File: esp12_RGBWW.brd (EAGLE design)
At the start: 53 x 47 mm, 36 parts, among them Q1 AOD2910SMD, Q2 AOD2910SMD, Q3 AOD2910SMD, Q4 AOD2910SMD, Q5 AOD2910SMD, U1 TPS5410DR

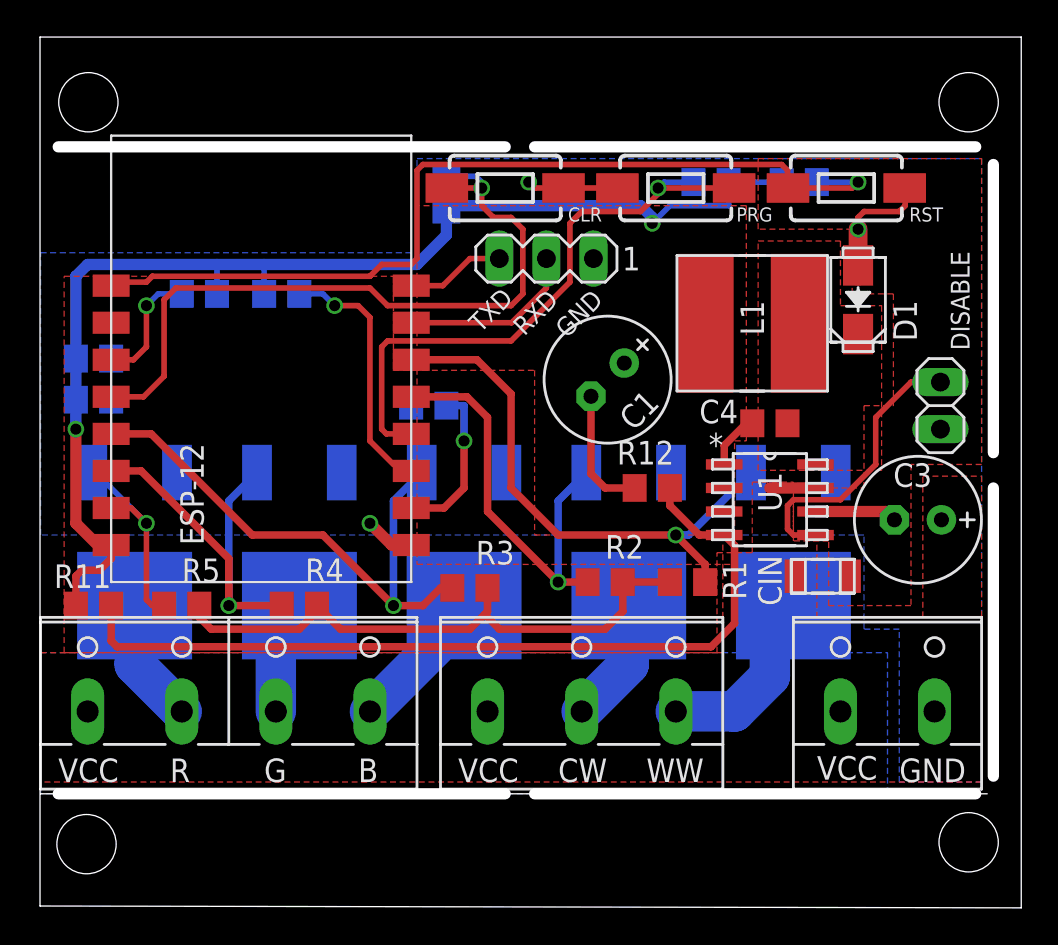
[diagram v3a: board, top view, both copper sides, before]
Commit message: minor changes
increased the size of the button text
very minor re-route of GPIO2 to resistor
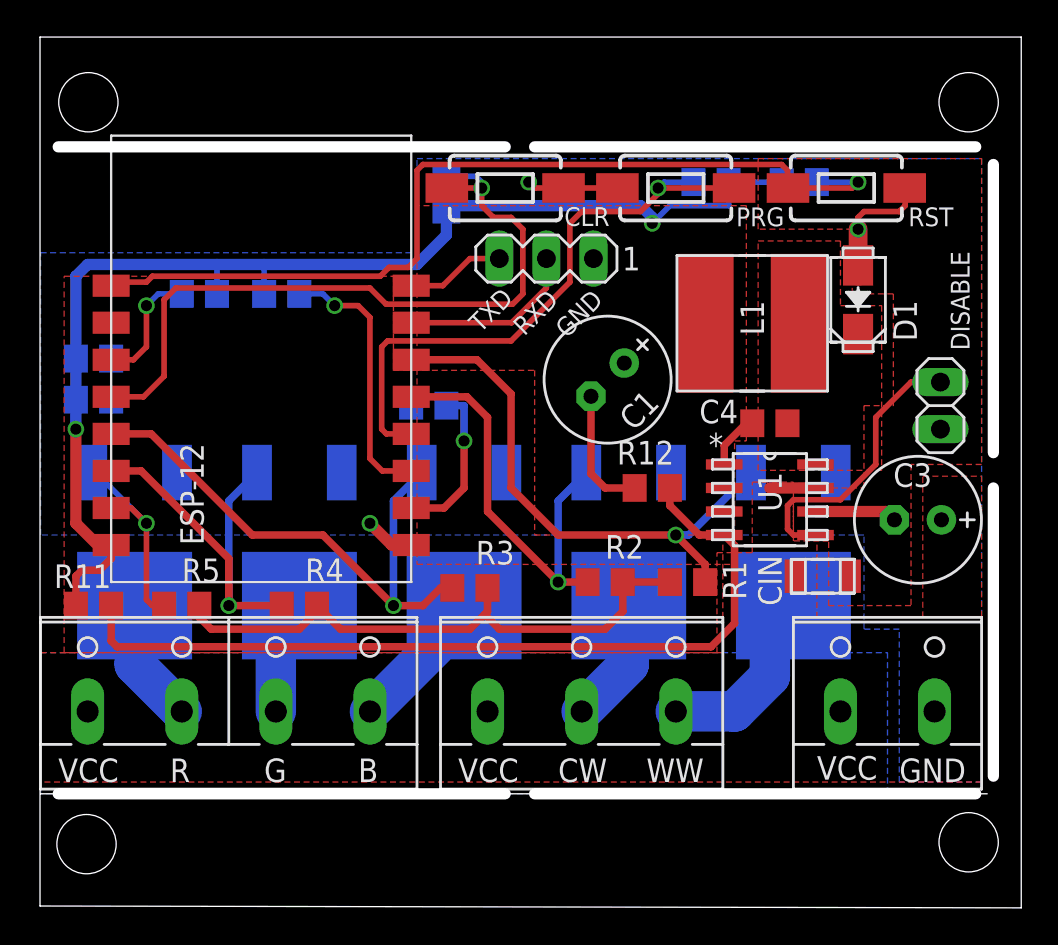
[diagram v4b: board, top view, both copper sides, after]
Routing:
- net G2: track 13.9 -> 14.5 mm
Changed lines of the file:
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@@
 <setting verticaltext="up"/>
 </settings>
-<grid distance="0.05" unitdist="inch" unit="inch" style="lines" multiple="1" display="no" altdistance="0.0125" altunitdist="inch" altunit="inch"/>
+<grid distance="0.05" unitdist="inch" unit="inch" style="lines" multiple="1" display="no" altdistance="0.003125" altunitdist="inch" altunit="inch"/>
 <layers>
 <layer number="1" name="Top" color="4" fill="1" visible="yes" active="yes"/>
@@
 <element name="C1" library="resistor" package="E2,5-7" value="440nF" x="29.3415125" y="22.3565125" smashed="yes" rot="R225">
 <attribute name="NAME" x="31.31716875" y="21.9075" size="1.27" layer="25" ratio="10" rot="R225"/>
-<attribute name="VALUE" x="24.941184375" y="22.4463125" size="1.27" layer="27" ratio="10" rot="R225"/>
+<attribute name="VALUE" x="29.148059375" y="25.8594375" size="1.27" layer="27" ratio="10" rot="R225"/>
 </element>
 <element name="C2" library="rcl" package="C0805" value="100n" x="1.5875" y="23.495" smashed="yes" rot="MR0">
@@
 <element name="CLR" library="SparkFun-Electromechanical" package="TACTILE-SWITCH-1101NE" value="" x="23.8125" y="32.7025" smashed="yes" rot="R180">
 <attribute name="PROD_ID" value="SWCH-00815" x="23.8125" y="32.7025" size="1.778" layer="27" rot="R180" display="off"/>
-<attribute name="NAME" x="29.035" y="31.655" size="0.762" layer="25" rot="R180"/>
+<attribute name="NAME" x="29.448125" y="31.670625" size="1.016" layer="25" rot="R180"/>
 <attribute name="VALUE" x="26.8125" y="35.4025" size="0.762" layer="27" rot="R180"/>
 </element>
@@
 <element name="PRG" library="SparkFun-Electromechanical" package="TACTILE-SWITCH-1101NE" value="" x="33.02" y="32.7025" smashed="yes" rot="R180">
 <attribute name="PROD_ID" value="SWCH-00815" x="33.02" y="32.7025" size="1.778" layer="27" rot="R180" display="off"/>
-<attribute name="NAME" x="38.2425" y="31.655" size="0.762" layer="25" rot="R180"/>
+<attribute name="NAME" x="38.8775" y="31.655" size="1.016" layer="25" rot="R180"/>
 <attribute name="VALUE" x="36.02" y="35.4025" size="0.762" layer="27" rot="R180"/>
 </element>
@@
 <element name="RST" library="SparkFun-Electromechanical" package="TACTILE-SWITCH-1101NE" value="" x="42.2275" y="32.7025" smashed="yes" rot="R180">
 <attribute name="PROD_ID" value="SWCH-00815" x="42.2275" y="32.7025" size="1.778" layer="27" rot="R180" display="off"/>
-<attribute name="NAME" x="47.45" y="31.655" size="0.762" layer="25" rot="R180"/>
+<attribute name="NAME" x="48.005625" y="31.655" size="1.016" layer="25" rot="R180"/>
 <attribute name="VALUE" x="45.2275" y="35.4025" size="0.762" layer="27" rot="R180"/>
 </element>
@@
 <contactref element="ESP-12" pad="3"/>
 <via x="14.605" y="26.3525" extent="1-16" drill="0.6"/>
-<wire x1="17.78" y1="17.78" x2="18.39" y2="17.78" width="0.254" layer="1"/>
-<wire x1="18.39" y1="17.78" x2="18.74" y2="17.43" width="0.254" layer="1"/>
-<wire x1="17.78" y1="17.78" x2="16.51" y2="19.05" width="0.3048" layer="1"/>
-<wire x1="16.51" y1="19.05" x2="16.51" y2="25.7175" width="0.3048" layer="1"/>
+<wire x1="16.51" y1="18.0975" x2="16.51" y2="25.7175" width="0.3048" layer="1"/>
 <wire x1="16.51" y1="25.7175" x2="15.875" y2="26.3525" width="0.3048" layer="1"/>
 <wire x1="15.875" y1="26.3525" x2="14.605" y2="26.3525" width="0.3048" layer="1"/>
 <wire x1="12.6975" y1="26.9875" x2="13.97" y2="26.9875" width="0.3048" layer="16"/>
 <wire x1="13.97" y1="26.9875" x2="14.605" y2="26.3525" width="0.3048" layer="16"/>
+<wire x1="18.74" y1="17.43" x2="17.1775" y2="17.43" width="0.3048" layer="1"/>
+<wire x1="17.1775" y1="17.43" x2="16.51" y2="18.0975" width="0.3048" layer="1"/>
 </signal>
 <signal name="PRG_S" class="5">
@@
 <via x="42.8625" y="33.02" extent="1-16" drill="0.6"/>
 <wire x1="39.0525" y1="33.045" x2="39.0775" y2="32.7025" width="0.3048" layer="1"/>
-<wire x1="16.51" y1="27.94" x2="4.7625" y2="27.94" width="0.3048" layer="1"/>
+<wire x1="17.065625" y1="27.94" x2="4.7625" y2="27.94" width="0.3048" layer="1"/>
 <wire x1="4.7625" y1="27.94" x2="4.445" y2="27.6225" width="0.3048" layer="1"/>
 <wire x1="4.445" y1="27.6225" x2="2.7325" y2="27.6225" width="0.3048" layer="1"/>
@@
 <wire x1="39.0525" y1="33.655" x2="39.0525" y2="32.7275" width="0.3048" layer="1"/>
 <wire x1="39.0525" y1="32.7275" x2="39.0775" y2="32.7025" width="0.3048" layer="1"/>
-<wire x1="16.51" y1="27.94" x2="17.145" y2="28.575" width="0.3048" layer="1"/>
-<wire x1="17.145" y1="28.575" x2="18.7325" y2="28.575" width="0.3048" layer="1"/>
-<wire x1="18.7325" y1="28.575" x2="19.05" y2="28.8925" width="0.3048" layer="1"/>
+<wire x1="17.065625" y1="27.94" x2="17.541875" y2="28.41625" width="0.3048" layer="1"/>
+<wire x1="17.541875" y1="28.41625" x2="18.57375" y2="28.41625" width="0.3048" layer="1"/>
+<wire x1="18.57375" y1="28.41625" x2="19.05" y2="28.8925" width="0.3048" layer="1"/>
 <wire x1="19.05" y1="28.8925" x2="19.05" y2="33.655" width="0.3048" layer="1"/>
 </signal>
@@
 <wire x1="5.3975" y1="26.67" x2="5.3975" y2="22.5425" width="0.3048" layer="1"/>
 <wire x1="20.6375" y1="32.6775" x2="20.6625" y2="32.7025" width="0.3048" layer="1"/>
-<wire x1="16.51" y1="27.305" x2="17.4625" y2="26.3525" width="0.3048" layer="1"/>
-<wire x1="17.4625" y1="26.3525" x2="24.13" y2="26.3525" width="0.3048" layer="1"/>
-<wire x1="24.13" y1="26.3525" x2="24.765" y2="26.9875" width="0.3048" layer="1"/>
+<wire x1="16.51" y1="27.305" x2="17.383125" y2="26.431875" width="0.3048" layer="1"/>
+<wire x1="17.383125" y1="26.431875" x2="24.209375" y2="26.431875" width="0.3048" layer="1"/>
+<wire x1="24.209375" y1="26.431875" x2="24.765" y2="26.9875" width="0.3048" layer="1"/>
 <wire x1="24.765" y1="26.9875" x2="24.765" y2="30.48" width="0.3048" layer="1"/>
 <wire x1="22.2275" y1="33.335" x2="22.5425" y2="33.02" width="0.3048" layer="16"/>

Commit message: added three accessible GPIOs
Added header pins for GPIOS 0,2 and 16 (which are all pulled high on board).
If using Tasmota, or if we make changes to the "native" firmware, those can be used to signal via MQTT and thus to provide "local" control
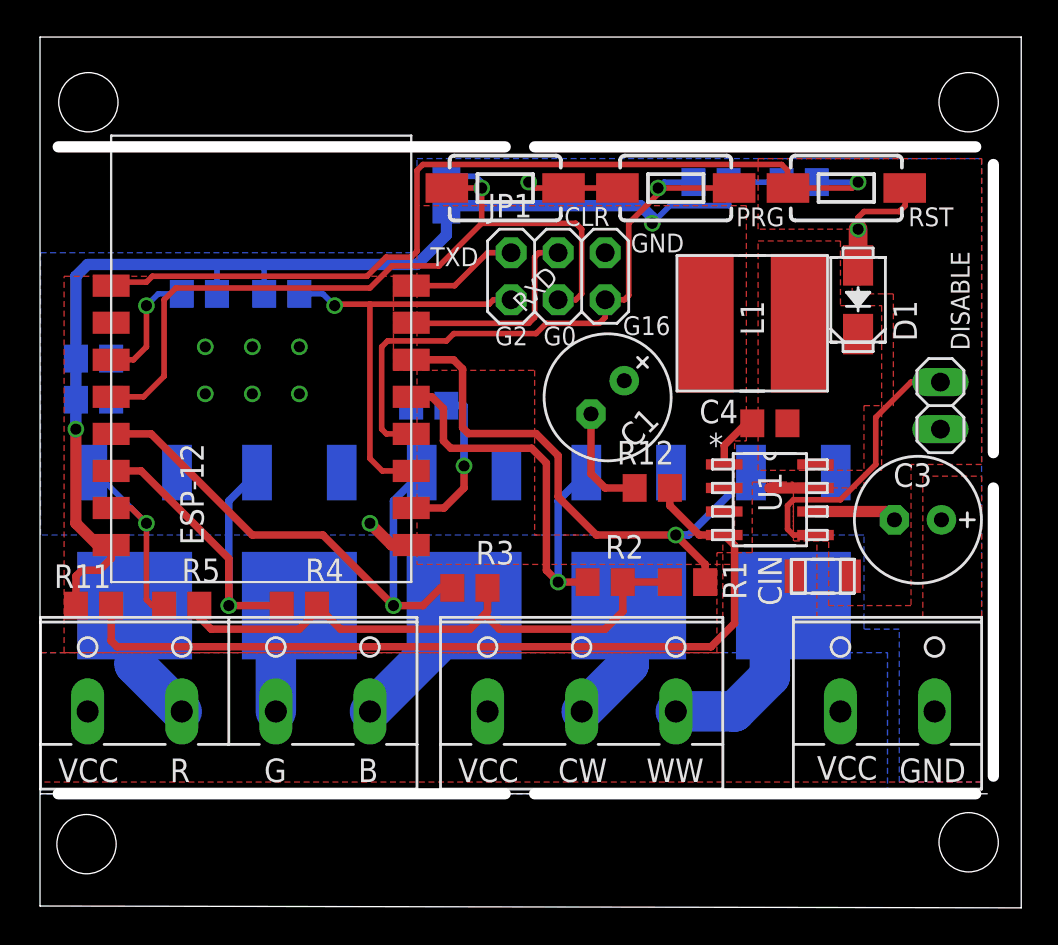
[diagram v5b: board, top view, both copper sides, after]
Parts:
- removed PROG: (no value), con-lstb:MA03-1
- added JP1: (no value), adafruit:2X03
- C1: value 440nF -> 470µF
- C3: value 240uF -> 220µF
- moved C1 0.95 mm to (29.3, 21.4)
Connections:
- net CLR_S: now also JP1.3
- net G2: now also JP1.1
- net GND: now also JP1.6; no longer PROG.1
- net PRG_S: now also JP1.5
- net RXD: now also JP1.4; no longer PROG.2
- net TXD: now also JP1.2; no longer PROG.3
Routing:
- net G2: track 14.5 -> 22.7 mm
- net CLR_S: track 39.4 -> 43.1 mm
- net RXD: track 9.66 -> 11.4 mm
- net RGB-CW: track 23.2 -> 24.6 mm
- net PRG_S: track 33.3 -> 34.3 mm
- net GND: track 59.3 -> 58.4 mm, vias 3 -> 9
- net TXD: track 5.36 -> 6.13 mm
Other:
- board text added: "G0"
- board text added: "G16"
- board text added: "G2"
